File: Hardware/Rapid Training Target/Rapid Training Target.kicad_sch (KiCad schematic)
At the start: 18 parts, among them U1 MIC5504-3.3YM5, U2 ESP32-C3-MINI-1-N4

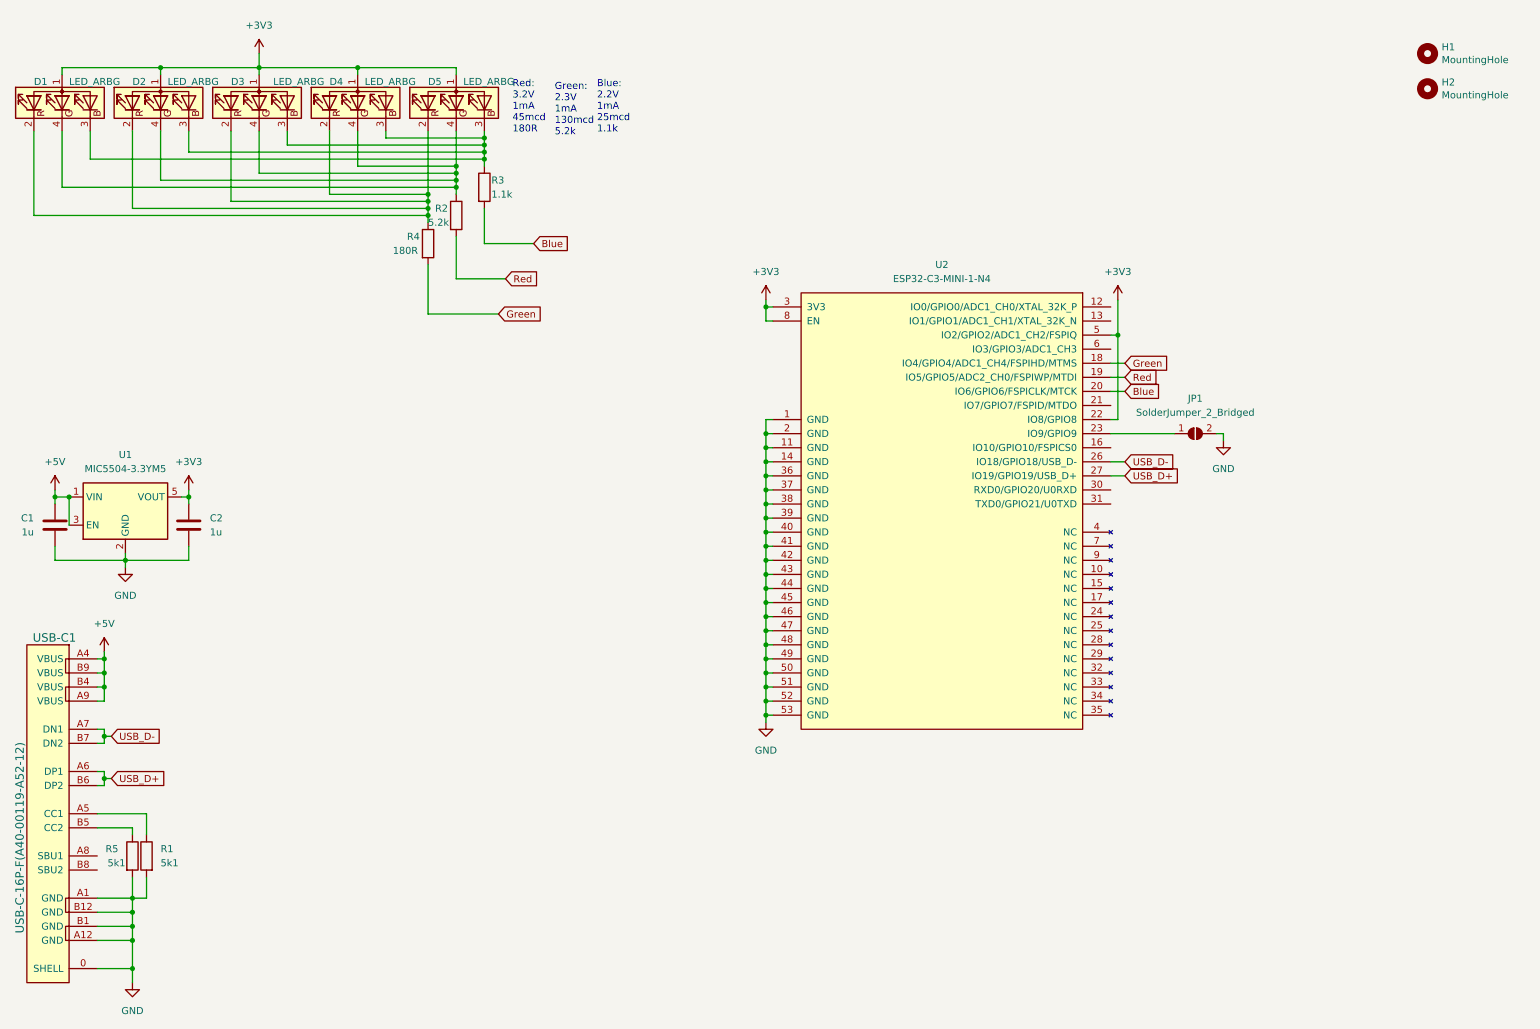
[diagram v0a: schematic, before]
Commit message: updated boot buttons on receiver
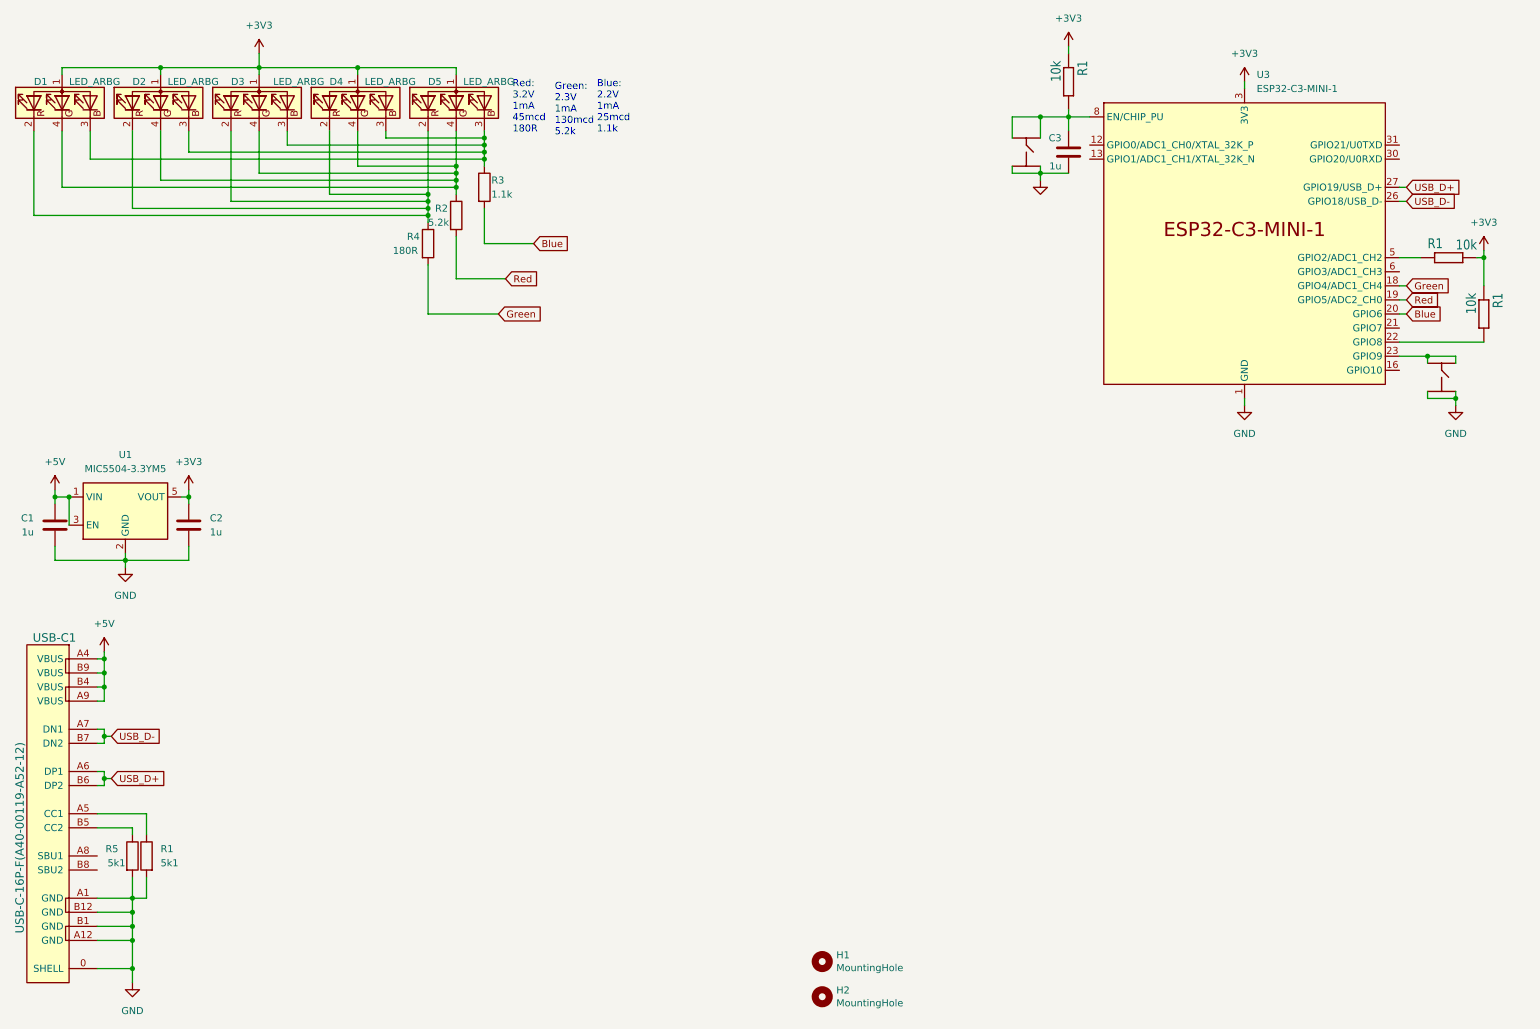
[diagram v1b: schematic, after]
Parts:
- removed JP1: SolderJumper_2_Bridged, Jumper:SolderJumper-2_P1.3mm_Open_RoundedPad1.0x1.5mm, symbol Jumper:SolderJumper_2_Open
- removed U2: ESP32-C3-MINI-1-N4, Personal:ESP32-­C3-­MINI­-1, symbol personal2:ESP32-­C3-­MINI­-1
- added C3: 1u, Capacitor_SMD:C_0603_1608Metric, symbol Device:C
- added R1 (x3): 10k, Resistor_SMD:R_0603_1608Metric, symbol picoclick_c3_v1.1-eagle-import:moekoe_rcl_R0402
- added U3: ESP32-C3-MINI-1, PCM_Espressif:ESP32-C3-MINI-1, symbol PCM_Espressif:ESP32-C3-MINI-1
- added s1, s2: BUTTON_4PIN_TS_1177, rapidtraining:TS-1177-C-B-B, symbol personal2:BUTTON_4PIN_TS_1177
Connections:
- net +3V3: now also R1.1, R1.1, R1.2, U3.3 (3V3)
- net Blue: now also U3.20 (GPIO6)
- net GND: now also C3.2, U3.1 (GND), U3.11 (GND), U3.14 (GND), U3.2 (GND), U3.36 (GND), U3.37 (GND), U3.38 (GND), U3.39 (GND), U3.40 (GND), U3.41 (GND), U3.42 (GND), U3.43 (GND), U3.44 (GND), U3.45 (GND), U3.46 (GND), U3.47 (GND), U3.48 (GND), U3.49 (GND), U3.50 (GND), U3.51 (GND), U3.52 (GND), U3.53 (GND), s1.P3 (3), s1.P4 (4), s2.P3 (3), s2.P4 (4)
- net Green: now also U3.18 (GPIO4/ADC1_CH4)
- net Red: now also U3.19 (GPIO5/ADC2_CH0)
- net USB_D+: now also U3.27 (GPIO19/USB_D+)
- net USB_D-: now also U3.26 (GPIO18/USB_D-)
- new net: U3.23 (GPIO9), s2.P1 (1), s2.P2 (2)
- new net: C3.1, R1.2, U3.8 (EN/CHIP_PU), s1.P1 (1), s1.P2 (2)
- new net: R1.2, U3.22 (GPIO8)
- new net: R1.1, U3.5 (GPIO2/ADC1_CH2)
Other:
- moved on the sheet: H1, H2
